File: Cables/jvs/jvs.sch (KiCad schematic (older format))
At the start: 19 parts, among them J1 DB25_Male, J2 Conn_01x01, J3 Conn_01x01, J4 Conn_01x01, J5 Conn_01x01, U1 THVD1450, U2 TPS6124x, U3 74AHC1G125

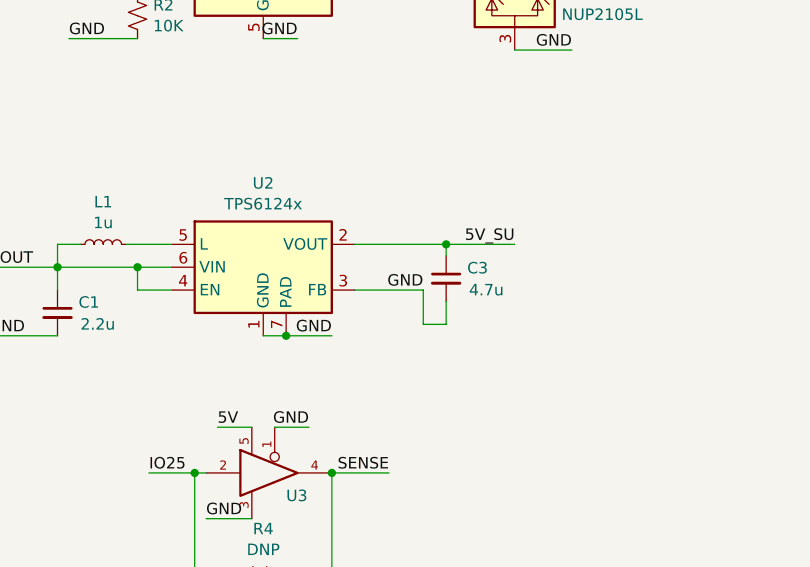
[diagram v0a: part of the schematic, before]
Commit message: [JVS] Fixup Step Up feedback wiring
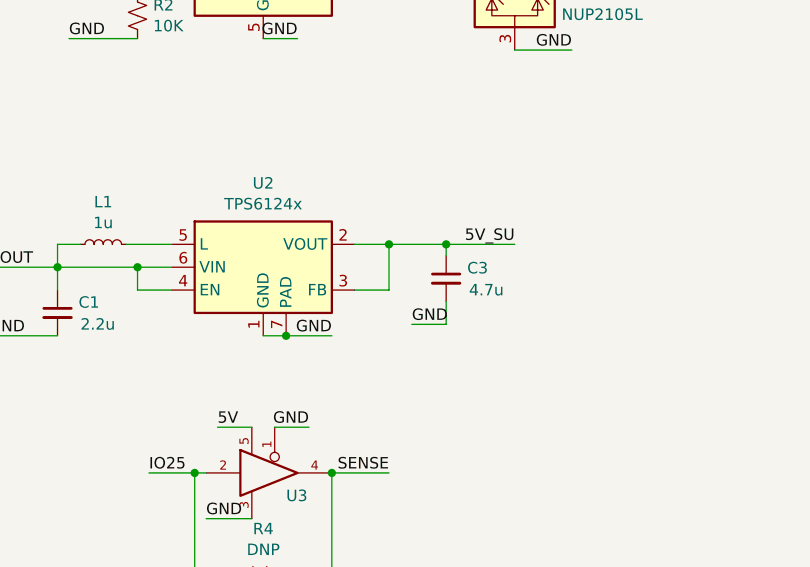
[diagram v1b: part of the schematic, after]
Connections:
- net 5V_SU: now also U2.3 (FB)
- net GND: no longer U2.3 (FB)
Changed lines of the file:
@@
 Sheet 1 1
 Title "BlueRetro - JVS cable adapter (RS485)"
-Date "2020-09-05"
-Rev "v1.0"
+Date "2020-09-25"
+Rev "v1.1"
 Comp ""
 Comment1 ""
@@
 GND
 Wire Wire Line
-	5500 4900 5800 4900
-Wire Wire Line
-	5500 4700 5900 4700
-Text Label 5800 4900 2    50   ~ 0
+	5500 4700 5650 4700
+Text Label 5750 5050 0    50   ~ 0
 GND
 Wire Wire Line
@@
 Wire Wire Line
 	5900 4950 5900 5050
-Wire Wire Line
-	5900 5050 5800 5050
-Wire Wire Line
-	5800 5050 5800 4900
 Text Label 4250 3400 0    50   ~ 0
 IO22
@@
 Text Label 3150 4850 2    50   ~ 0
 IO25
+Wire Wire Line
+	5500 4900 5650 4900
+Wire Wire Line
+	5650 4900 5650 4700
+Connection ~ 5650 4700
+Wire Wire Line
+	5650 4700 5900 4700
+Wire Wire Line
+	5900 5050 5750 5050
 $EndSCHEMATC
